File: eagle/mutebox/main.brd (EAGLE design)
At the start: 127 x 50.8 mm, 31 parts, among them IC1 6N138S-TA1, IC2 6N138S-TA1, SW1 RK09D1130C2P

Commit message: mutebox
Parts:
- removed CONN_MIDI, CONN_SCS: (no value), microbuilder:2X05
- removed S1: EG1821-ND + EG1821-ND, og-switch:B3F-40XX
- removed S2, S3, S4, S5: (no value), og-switch:B3F-40XX
- removed SW1: RK09D1130C2P, switch-alps:ALPS_EC12E_SW
- added U$1: STM32F4-DISCOVERY, STM32F4-DISCOVERY:STM32F4-DISCOVERY
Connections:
- removed net MIDI_IN3: CONN_MIDI.6
- removed net MIDI_IN4: CONN_MIDI.5
- removed net MIDI_OUT3: CONN_MIDI.10
- removed net MIDI_OUT4: CONN_MIDI.9
- removed net SCS_D0: CONN_SCS.3, SW1.A
- removed net SCS_D1: CONN_SCS.4, SW1.B
- removed net SCS_D2: CONN_SCS.5, S5.1, S5.2
- removed net SCS_D3: CONN_SCS.6, S4.1, S4.2
- removed net SCS_D4: CONN_SCS.7, S3.1, S3.2
- removed net SCS_D5: CONN_SCS.8, S2.1, S2.2
- removed net SCS_D6: CONN_SCS.9, S1.1, S1.2
- removed net SCS_D7: CONN_SCS.10, SW1.E
- net 3.3V: now also U$1.P$3, U$1.P$4, U$1.P$55, U$1.P$56, U$1.P$72; no longer CONN_SCS.2
- net 5.0V: now also U$1.P$53, U$1.P$54; no longer CONN_MIDI.2
- net GND: now also U$1.P$1, U$1.P$100, U$1.P$2, U$1.P$23, U$1.P$49, U$1.P$5, U$1.P$50, U$1.P$51, U$1.P$52, U$1.P$99; no longer CONN_MIDI.1, CONN_SCS.1, S1.3, S1.4, S2.3, S2.4, S3.3, S3.4, S4.3, S4.4, S5.3, S5.4, SW1.C, SW1.D
- net MIDI_IN1: now also U$1.P$13; no longer CONN_MIDI.4
- net MIDI_IN2: now also U$1.P$41; no longer CONN_MIDI.3
- net MIDI_OUT1: now also U$1.P$14; no longer CONN_MIDI.8
- net MIDI_OUT2: now also U$1.P$40; no longer CONN_MIDI.7

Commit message: wip
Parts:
- removed LCD1: NHD-C0220AA-FSW-FTW, NHD-C0220AA-FSW-FTW:NHD-C0220AA-FSW-FTW
- moved U$1 85.1 mm to (39.4, 43.2)
- moved MIDI_IN2 67.2 mm to (101.6, 76.2)
- moved MIDI_OUT2 67.2 mm to (81.3, 76.2)
- moved MIDI_IN1 38.7 mm to (50.8, 76.2)
- moved MIDI_OUT1 38.7 mm to (30.5, 76.2)
- moved H1 25.4 mm to (2.54, 73.7)
- moved H2 25.4 mm to (124.5, 73.7)
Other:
- board size 127 x 50.8 mm -> 127 x 76.2 mm

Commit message: muteboxwip
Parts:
- added B_CONN1, B_CONN2, CONN_SCS, P_CONN1, P_CONN2: (no value), microbuilder:2X05
- added C1, C2: 100nF, microbuilder:0603
- added IC3, IC4: 74HCT541DW, 74xx-eu:SO20W
- added JP1: (no value), microbuilder:2X08
- R10, R5: value 4.7K -> 1K
- R4, R9: value 1K -> 4.7K
- moved IC1 200.9 mm to (107.7, 6.86), turned to 90 degrees
- moved R10 183.6 mm to (91.2, 6.86), flipped to the bottom, turned to 180 degrees
- moved R5 183.1 mm to (109.7, 6.86), flipped to the bottom, turned to 180 degrees
- moved R9 176.6 mm to (87.1, 6.86), flipped to the bottom
- moved R4 176.1 mm to (105.7, 6.86), flipped to the bottom
- moved R1 148.7 mm to (107.7, 60.7), flipped to the bottom
- moved IC2 142.0 mm to (89.2, 6.35), turned to 90 degrees
- moved R3 135.8 mm to (86.6, 59.7), flipped to the bottom, turned to 90 degrees
- moved D1 124.3 mm to (91.2, 59.2), flipped to the bottom, turned to 90 degrees
- moved R6 116.9 mm to (55.9, 60.2), flipped to the bottom
- moved R2 116.1 mm to (70.4, 60.5), flipped to the bottom, turned to 180 degrees
- moved R8 105.6 mm to (36.6, 60.5), flipped to the bottom
- moved R7 85.0 mm to (18.5, 60.2), flipped to the bottom, turned to 180 degrees
- moved D2 81.0 mm to (40.6, 59.4), flipped to the bottom, turned to 90 degrees
- moved MIDI_OUT2 53.3 mm to (27.9, 76.2)
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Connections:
- new net LCD_B+: JP1.1
- new net LCD_B-: JP1.2
- new net LCD_D0: JP1.9
- new net LCD_D1: JP1.10
- new net LCD_D2: JP1.7
- new net LCD_D3: JP1.8
- new net LCD_D4: JP1.5
- new net LCD_D5: JP1.6
- new net LCD_D6: JP1.3
- new net LCD_D7: JP1.4
- new net LCD_E: JP1.12
- new net LCD_RS: JP1.14
- new net LCD_RW: JP1.11
- new net LCD_V0: JP1.13
- new net LCD_VD: JP1.16
- new net LCD_VS: JP1.15
- new net MOD1_BTN_CS1: B_CONN1.9, IC3.13
- new net MOD1_BTN_CS2: B_CONN1.10, IC3.14
- new net MOD1_BTN_SC: B_CONN1.7, B_CONN1.8, IC3.12
- new net MOD1_BTN_SI: B_CONN1.5
- new net MOD1_BTN_SO: B_CONN1.6, IC3.11
- new net MOD1_POT_CS1: IC3.17, P_CONN1.10
- new net MOD1_POT_CS2: IC3.18, P_CONN1.9
- new net MOD1_POT_SC: IC3.16, P_CONN1.7, P_CONN1.8
- new net MOD1_POT_SO: IC3.15, P_CONN1.6
- new net MOD2_BTN_CS1: B_CONN2.9, IC4.13
- new net MOD2_BTN_CS2: B_CONN2.10, IC4.14
- new net MOD2_BTN_SC: B_CONN2.7, B_CONN2.8, IC4.12
- new net MOD2_BTN_SO: B_CONN2.6, IC4.11
- new net MOD2_POT_CS1: IC4.17, P_CONN2.10
- new net MOD2_POT_CS2: IC4.18, P_CONN2.9
- new net MOD2_POT_SC: IC4.16, P_CONN2.7, P_CONN2.8
- new net MOD2_POT_SO: IC4.15, P_CONN2.6
- new net PA15: IC3.3
- new net PB12: IC3.7
- new net PB13: IC3.8, IC4.8
- new net PB15: IC3.9, IC4.9
- new net PB3: IC3.4, IC4.4
- new net PB5: IC3.5, IC4.5
- new net PB8: IC3.2
- new net PC13: IC4.2
- new net PC14: IC4.3
- new net PD10: IC3.6
- new net PE4: IC4.6
- new net PE5: IC4.7
- new net PE8: CONN_SCS.3
- new net PE9: CONN_SCS.4
- new net SCS_D2: CONN_SCS.5
- new net SCS_D3: CONN_SCS.6
- new net SCS_D4: CONN_SCS.7
- new net SCS_D5: CONN_SCS.8
- new net SCS_D6: CONN_SCS.9
- new net SCS_D7: CONN_SCS.10
- new net TODO_SI: B_CONN2.5, P_CONN1.5, P_CONN2.5
- net 3.3V: now also CONN_SCS.2; no longer U$1.P$3, U$1.P$4, U$1.P$55, U$1.P$56, U$1.P$72
- net 5.0V: now also B_CONN1.3, B_CONN1.4, B_CONN2.3, B_CONN2.4, C1.1, C2.1, IC3.20, IC4.20, P_CONN1.3, P_CONN1.4, P_CONN2.3, P_CONN2.4; no longer U$1.P$53, U$1.P$54
- net GND: now also B_CONN1.1, B_CONN1.2, B_CONN2.1, B_CONN2.2, C1.2, C2.2, CONN_SCS.1, IC3.1, IC3.10, IC3.19, IC4.1, IC4.10, IC4.19, P_CONN1.1, P_CONN1.2, P_CONN2.1, P_CONN2.2; no longer U$1.P$1, U$1.P$100, U$1.P$2, U$1.P$23, U$1.P$49, U$1.P$5, U$1.P$50, U$1.P$51, U$1.P$52, U$1.P$99
- net MIDI_IN1: no longer U$1.P$13
- net MIDI_IN2: no longer U$1.P$41
- net MIDI_OUT1: no longer U$1.P$14
- net MIDI_OUT2: no longer U$1.P$40
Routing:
- added copper zone on layer 1, net 5.0V
- added copper zone on layer 16, net GND

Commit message: muteboxwip
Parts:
- moved JP1 51.5 mm to (92.2, 24.6)
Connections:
- removed net MOD1_BTN_SI: B_CONN1.5
- removed net PE8: CONN_SCS.3
- removed net PE9: CONN_SCS.4
- removed net TODO_SI: B_CONN2.5, P_CONN1.5, P_CONN2.5
- new net PB14: B_CONN1.5, B_CONN2.5, U$1.P$38
- new net PB4: P_CONN1.5, P_CONN2.5, U$1.P$75
- new net PE3: U$1.P$66
- new net SCS_D0: CONN_SCS.3, U$1.P$26
- new net SCS_D1: CONN_SCS.4, U$1.P$27
- net 3.3V: now also U$1.P$3, U$1.P$4, U$1.P$55, U$1.P$56, U$1.P$72
- net 5.0V: now also U$1.P$53, U$1.P$54
- net GND: now also U$1.P$1, U$1.P$100, U$1.P$2, U$1.P$23, U$1.P$49, U$1.P$5, U$1.P$50, U$1.P$51, U$1.P$52, U$1.P$99
- net MIDI_IN1: now also U$1.P$13
- net MIDI_IN2: now also U$1.P$41
- net MIDI_OUT1: now also U$1.P$14
- net MIDI_OUT2: now also U$1.P$40
- net PA15: now also U$1.P$90
- net PB12: now also U$1.P$36
- net PB13: now also U$1.P$37
- net PB15: now also U$1.P$39
- net PB3: now also U$1.P$78
- net PB5: now also U$1.P$76
- net PB8: now also U$1.P$69
- net PC13: now also U$1.P$62
- net PC14: now also U$1.P$59
- net PD10: now also U$1.P$42
- net PE4: now also U$1.P$63
- net PE5: now also U$1.P$64
- net SCS_D2: now also U$1.P$28
- net SCS_D3: now also U$1.P$29
- net SCS_D4: now also U$1.P$30
- net SCS_D5: now also U$1.P$31
- net SCS_D6: now also U$1.P$32
- net SCS_D7: now also U$1.P$33

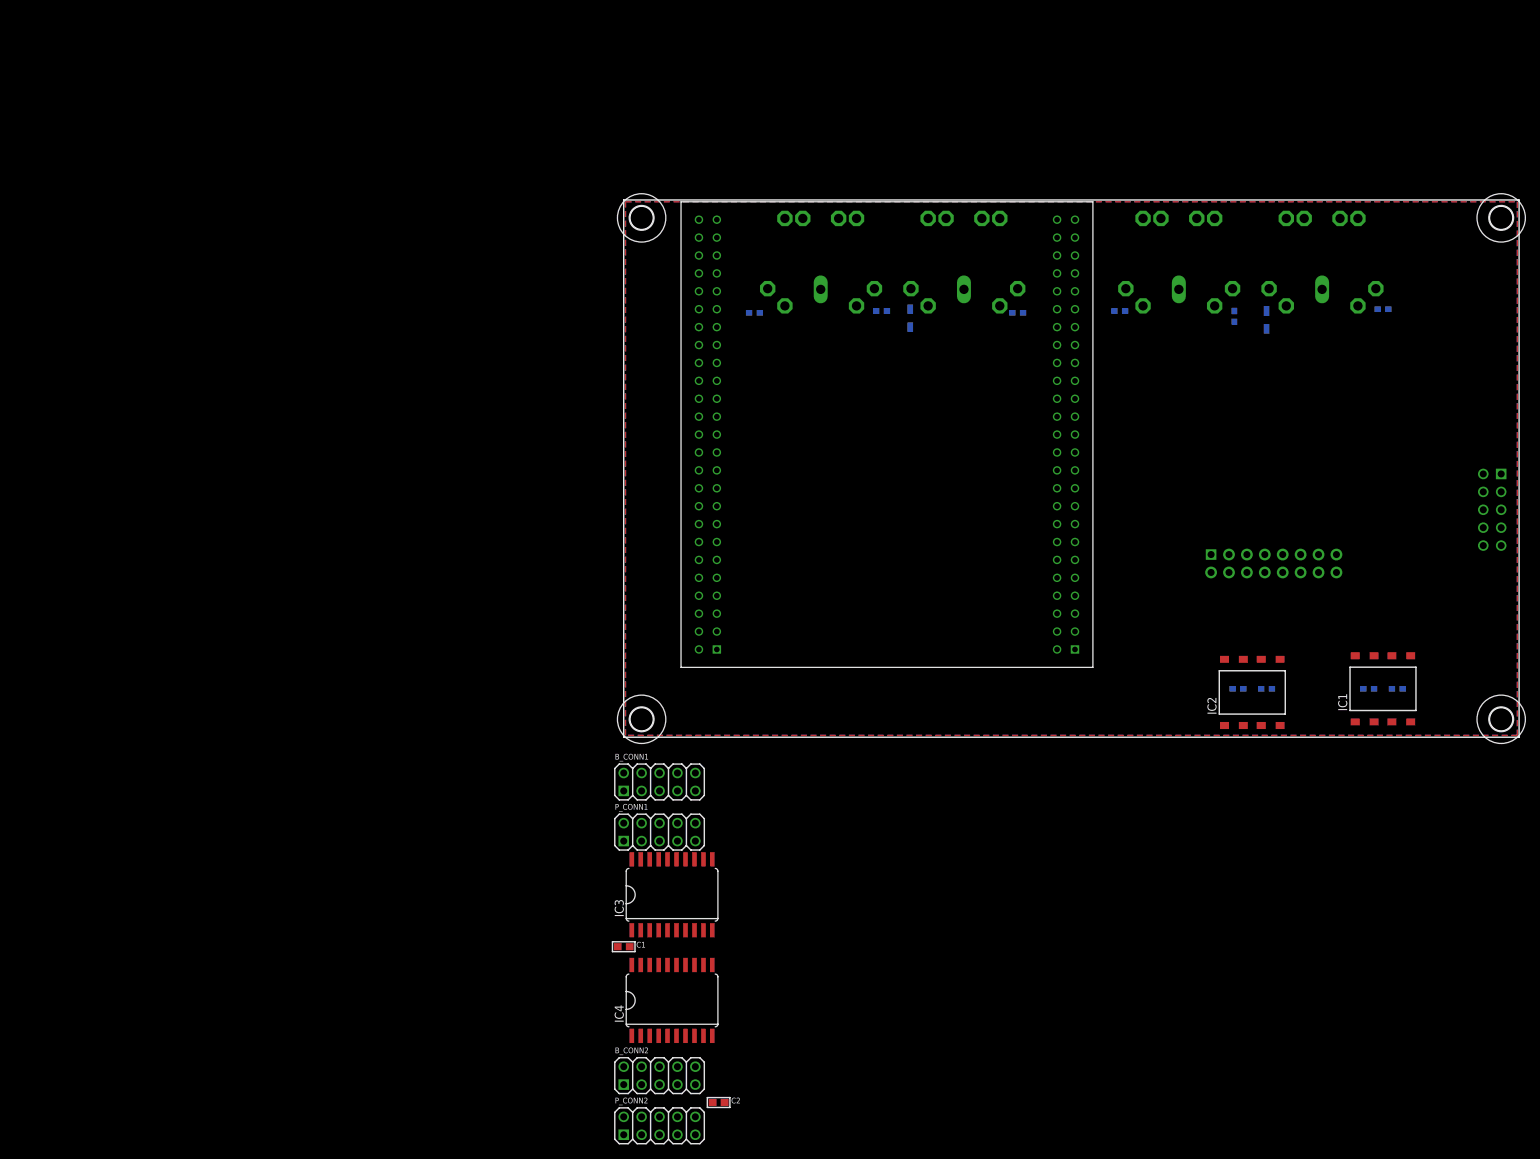
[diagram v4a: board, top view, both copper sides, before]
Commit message: mutebox main: shrouded connectors
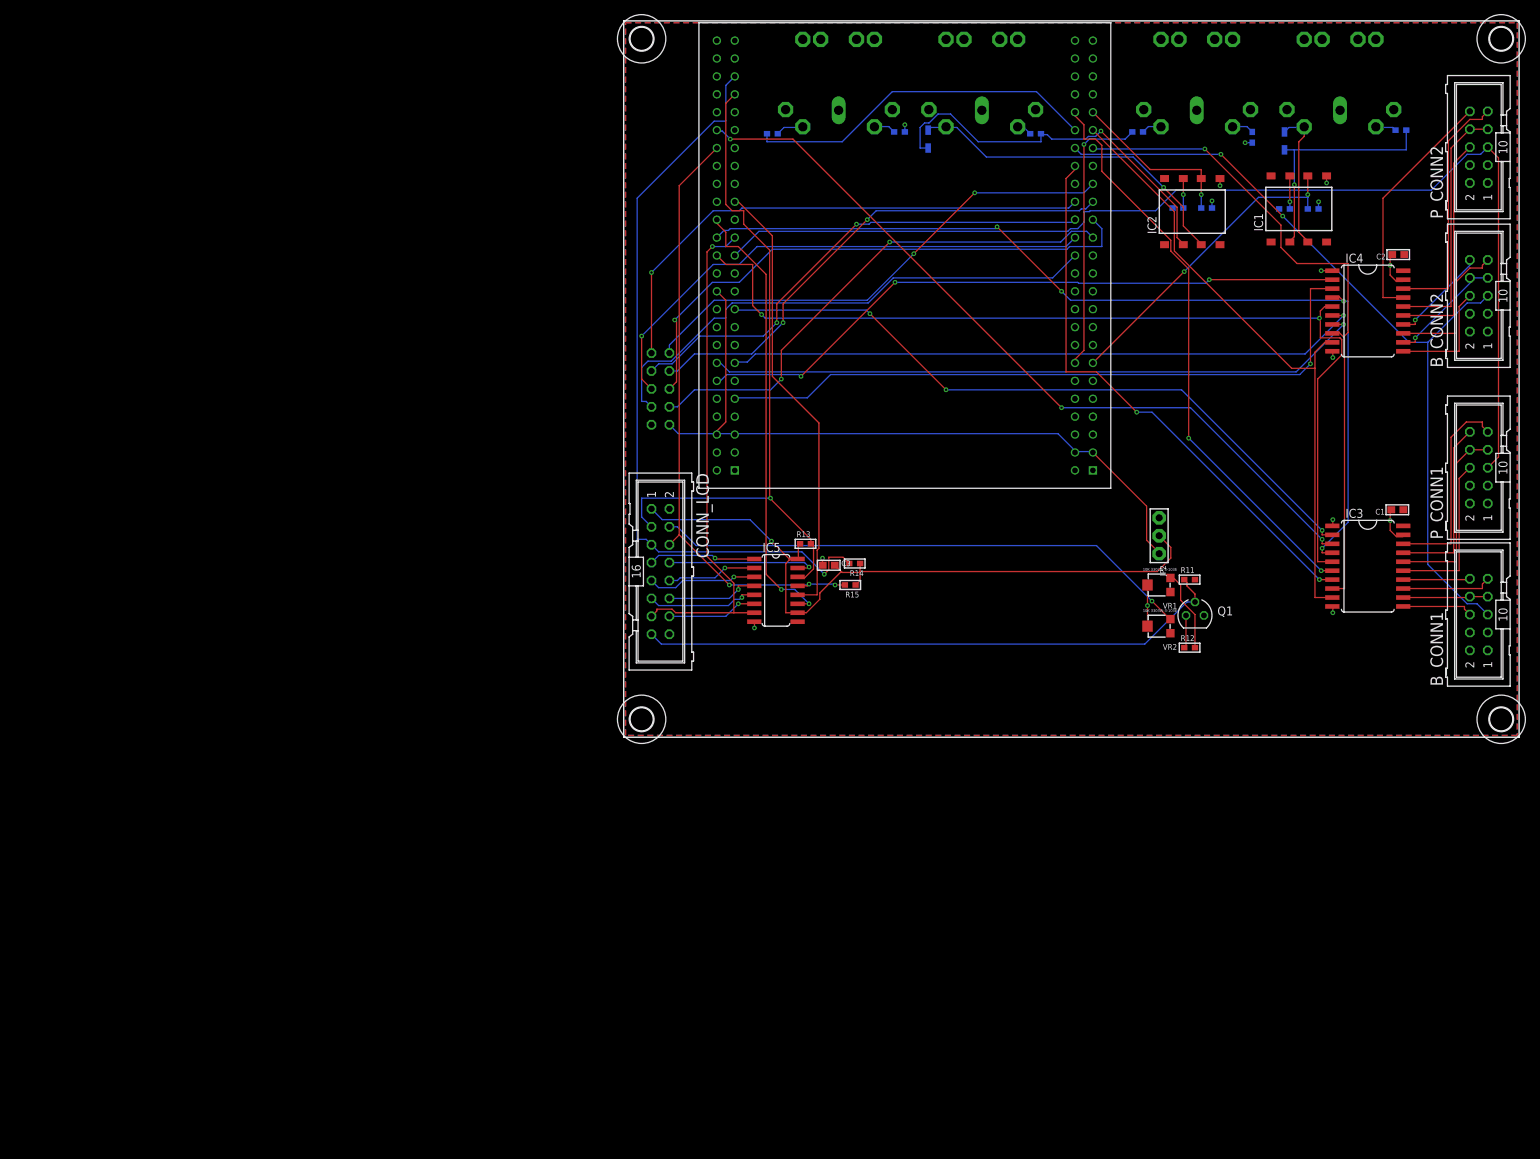
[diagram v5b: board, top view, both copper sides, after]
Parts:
- removed JP1: (no value), microbuilder:2X08
- added C3: 100nF, microbuilder:0603
- added CONN_LCD: (no value), con-harting-ml:ML16
- added IC5: 74HC595D, 74xx-eu:SO16
- added JP2: (no value), microbuilder:JUMPER3
- added Q1: BC337, transistor-small-signal:SOT54A
- added R11: 10K, microbuilder:_0603
- added R12, R13, R14, R15: 1K, microbuilder:_0603
- added VR1, VR2: 10K 3303W-3-103E, microbuilder:TRIMPOT_BOURNS3MM
- B_CONN1, B_CONN2, CONN_SCS, P_CONN1, P_CONN2: device microbuilder:2X05 -> con-harting-ml:ML10
- moved P_CONN2 181.0 mm to (121.3, 83.7), turned to 90 degrees
- moved B_CONN2 160.4 mm to (121.3, 62.6), turned to 90 degrees
- moved C2 154.1 mm to (109.9, 68.5), turned to 180 degrees
- moved IC4 138.9 mm to (105.5, 60.5), turned to 270 degrees
- moved P_CONN1 127.2 mm to (121.3, 38.2), turned to 90 degrees
- moved C1 126.0 mm to (109.7, 32.3), turned to 180 degrees
- moved CONN_SCS 119.2 mm to (5.21, 49.4), turned to 90 degrees
- moved B_CONN1 118.6 mm to (121.3, 17.4), turned to 90 degrees
- moved IC3 109.1 mm to (105.5, 24.3), turned to 270 degrees
- moved IC1 69.1 mm to (95.8, 74.9)
- moved R4 69.1 mm to (93.7, 74.9)
- moved R5 69.1 mm to (97.8, 74.9)
- moved IC2 68.7 mm to (80.6, 74.5)
- moved R10 68.7 mm to (82.7, 75.1)
- moved R9 68.7 mm to (78.6, 75.1)
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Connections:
- removed net LCD_B+: JP1.1
- removed net LCD_E: JP1.12
- removed net LCD_VS: JP1.15
- removed net PE3: U$1.P$66
- new net LCD_E1: CONN_LCD.5, R14.2, U$1.P$95
- new net LCD_SER_RCLK: IC5.12, U$1.P$81
- new net LCD_SER_SCLK: IC5.11, U$1.P$80
- new net N$14: R12.2, VR1.S
- new net N$7: Q1.C, R12.1
- net 3.3V: now also JP2.3
- net 5.0V: now also CONN_LCD.16, JP2.1, R11.2, VR1.A, VR2.A
- net GND: now also C3.1, CONN_LCD.2, IC5.8, Q1.E, VR1.E, VR2.E
- net LCD_B-: now also CONN_LCD.15, Q1.B, R11.1; no longer JP1.2
- net LCD_D0: now also CONN_LCD.8, IC5.15; no longer JP1.9
- net LCD_D1: now also CONN_LCD.7, IC5.1; no longer JP1.10
- net LCD_D2: now also CONN_LCD.10, IC5.2; no longer JP1.7
- net LCD_D3: now also CONN_LCD.9, IC5.3; no longer JP1.8
- net LCD_D4: now also CONN_LCD.12, IC5.4; no longer JP1.5
- net LCD_D5: now also CONN_LCD.11, IC5.5; no longer JP1.6
- net LCD_D6: now also CONN_LCD.14, IC5.6; no longer JP1.3
- net LCD_D7: now also CONN_LCD.13, IC5.7, U$1.P$77; no longer JP1.4
- net LCD_RS: now also CONN_LCD.3, IC5.14, R13.2, U$1.P$93; no longer JP1.14
- net LCD_RW: now also CONN_LCD.6, IC5.13, R15.2, U$1.P$88; no longer JP1.11
- net LCD_V0: now also CONN_LCD.4, VR2.S; no longer JP1.13
- net LCD_VD: now also C3.2, CONN_LCD.1, IC5.10, IC5.16, JP2.2, R13.1, R14.1, R15.1; no longer JP1.16
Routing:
- net PB4: track 0.00 -> 160.8 mm
- net PB5: track 0.00 -> 136.6 mm, vias 0 -> 2
- net PB3: track 0.00 -> 135.2 mm, vias 0 -> 4
- net PB14: track 0.00 -> 115.6 mm, vias 0 -> 2
- net PA15: track 0.00 -> 112.0 mm, vias 0 -> 3
- net LCD_E1: track 0.00 -> 106.9 mm, vias 0 -> 1
- net 3.3V: track 0.00 -> 101.9 mm
- net LCD_VD: track 0.00 -> 100.8 mm, vias 0 -> 1
- net LCD_RS: track 0.00 -> 99.9 mm, vias 0 -> 1
- net PB8: track 0.00 -> 98.4 mm, vias 0 -> 3
- net PC14: track 0.00 -> 97.5 mm, vias 0 -> 1
- net PB13: track 0.00 -> 95.0 mm, vias 0 -> 1
- net PE5: track 0.00 -> 93.8 mm, vias 0 -> 1
- net PC13: track 0.00 -> 93.6 mm, vias 0 -> 3
- net PE4: track 0.00 -> 90.7 mm, vias 0 -> 1
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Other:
- board size 127 x 76.2 mm -> 127 x 101.6 mm

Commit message: wip
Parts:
- added H5, H6, H7, H8: MOUNT-HOLE3.3, holes:3,3
- moved CONN_SCS 115.4 mm to (119.8, 63.1)
- moved P_CONN2 64.3 mm to (106.2, 21.2)
- moved R11 59.9 mm to (20.3, 21.8), flipped to the bottom
- moved JP2 56.5 mm to (19.4, 27.7), flipped to the bottom, turned to 90 degrees
- moved P_CONN1 53.2 mm to (79.6, 5.21), turned to 0 degrees
- moved VR1 52.9 mm to (23.4, 16.0), flipped to the bottom, turned to 180 degrees
- moved Q1 51.9 mm to (29.2, 19.2), flipped to the bottom, turned to 270 degrees
- moved C1 51.0 mm to (66.5, 5.21), flipped to the bottom, turned to 0 degrees
- moved R12 48.0 mm to (32.8, 19.6), flipped to the bottom, turned to 270 degrees
- moved VR2 47.1 mm to (29.0, 12.8), flipped to the bottom, turned to 180 degrees
- moved C2 46.2 mm to (94.0, 25.0), flipped to the bottom, turned to 0 degrees
- moved IC3 44.5 mm to (62.4, 13.5), flipped to the bottom, turned to 90 degrees
- moved IC5 43.2 mm to (23.7, 64.0), flipped to the bottom
- moved B_CONN2 41.5 mm to (118.0, 21.2)
- moved CONN_LCD 41.5 mm to (5.08, 65.0)
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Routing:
- net LCD_SER_RCLK: track 63.9 -> 4.98 mm
- net LCD_SER_SCLK: track 63.7 -> 8.05 mm, vias 2 -> 0
- net PB14: track 115.6 -> 160.8 mm, vias 2 -> 3
- net LCD_D7: track 72.9 -> 27.9 mm, vias 1 -> 0
- net 5.0V: track 4.06 -> 45.8 mm, vias 4 -> 5
- net 3.3V: track 101.9 -> 143.5 mm, vias 0 -> 1
- net PB8: track 98.4 -> 57.7 mm, vias 3 -> 2
- net LCD_D2: track 12.8 -> 52.5 mm, vias 1 -> 2
- net MOD1_BTN_CS2: track 9.58 -> 49.1 mm, vias 0 -> 1
- net PB3: track 135.2 -> 102.4 mm, vias 4 -> 5
- net MOD1_BTN_SC: track 12.1 -> 44.7 mm
- net MOD1_BTN_CS1: track 12.9 -> 45.0 mm, vias 0 -> 1
- net MOD1_BTN_SO: track 10.1 -> 41.7 mm, vias 0 -> 2
- net PB5: track 136.6 -> 105.9 mm, vias 2 -> 3
- net GND: track 25.3 -> 0.00 mm, vias 11 -> 0
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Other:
- board size 127 x 101.6 mm -> 127 x 88.9 mm

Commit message: wip
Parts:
- moved R13 67.0 mm to (3.56, 80.5), flipped to the top, turned to 180 degrees
- moved R15 30.8 mm to (4.19, 47.8), flipped to the top
- moved R14 30.5 mm to (3.05, 49.5), flipped to the top
- moved D1 16.0 mm to (109.7, 71.8), turned to 0 degrees
- moved D2 15.5 mm to (58.7, 70.9), turned to 0 degrees
- moved VR2 14.1 mm to (16.5, 19.4), turned to 90 degrees
- moved R4 7.91 mm to (99.9, 68.3), turned to 180 degrees
- moved R12 7.29 mm to (26.0, 16.8), turned to 90 degrees
- moved R9 6.60 mm to (85.2, 69.1)
- moved R5 2.05 mm to (95.2, 68.3)
- moved R10 1.53 mm to (80.1, 68.2)
- moved Q1 1.02 mm to (29.7, 18.3)
- moved R6 0.76 mm to (59.2, 72.9)
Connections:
- net 5.0V: now also U$1.P$94; no longer VR2.A
- net GND: now also VR2.A; no longer VR2.E
- net LCD_VD: now also VR2.E
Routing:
- net LCD_RS: track 100.8 -> 43.3 mm, vias 4 -> 1
- net LCD_VD: track 89.3 -> 128.2 mm
- net LCD_E1: track 81.8 -> 44.6 mm
- net LCD_RW: track 84.1 -> 48.6 mm, vias 3 -> 0
- net N$11: track 54.2 -> 30.7 mm
- net 5.0V: track 45.8 -> 22.8 mm, vias 5 -> 8
- net LCD_V0: track 73.9 -> 55.8 mm
- net N$5: track 20.3 -> 30.0 mm
- net PB4: track 181.1 -> 171.4 mm, vias 3 -> 1
- net PB14: track 160.8 -> 151.3 mm, vias 3 -> 2
- net N$14: track 8.91 -> 1.76 mm
- net N$4: track 31.5 -> 27.0 mm
- net N$6: track 5.94 -> 2.74 mm, vias 2 -> 0
- net N$12: track 44.8 -> 41.7 mm
- net PB3: track 102.4 -> 105.0 mm
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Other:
- board text added: "MuteBox Main PCB v1.0 (c) Eran Rundstein, 2014"
